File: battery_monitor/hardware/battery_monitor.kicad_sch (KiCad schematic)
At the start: 51 parts, among them J1 VEHICLE, J2 EXT_NTC, J3 DPDT_SENSE_POLE, U1 TPS7A1633AQDGNRQ1, U2 TLV7034QPWRQ1, U3 MDBT50Q-1MV2 (logical symbol)

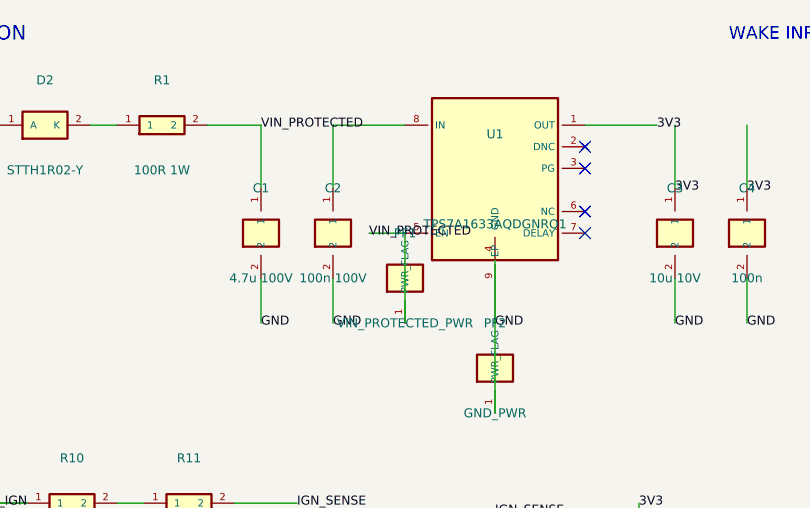
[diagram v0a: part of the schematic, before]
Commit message: Apply KiCad ERC fixes
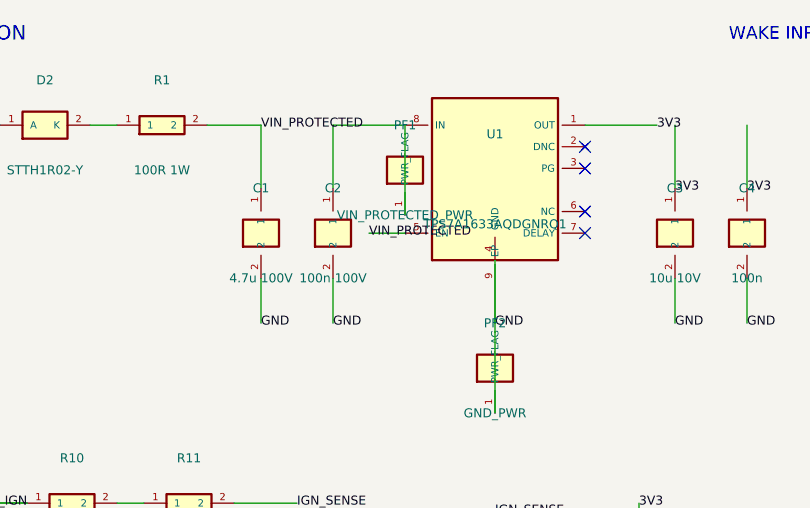
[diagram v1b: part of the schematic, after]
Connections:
- net VIN_PROTECTED: no longer PF1.1 (PWR_FLAG)
- net at C2.1, U1.8 (IN): now also PF1.1 (PWR_FLAG)
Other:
- moved on the sheet: PF1
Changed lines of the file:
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@@
   (wire (pts (xy 92 45) (xy 92 52)) (stroke (width 0) (type default)))
   (wire (pts (xy 92 48) (xy 92 52)) (stroke (width 0) (type default)))
-  (wire (pts (xy 82 42) (xy 82 52)) (stroke (width 0) (type default)))
+  (wire (pts (xy 82 30) (xy 82 40)) (stroke (width 0) (type default)))
   (wire (pts (xy 92 52) (xy 92 62)) (stroke (width 0) (type default)))
   (wire (pts (xy 112 37) (xy 112 30)) (stroke (width 0) (type default)))
@@
     (instances (project "battery_monitor" (path "/9c88e388-d519-50ad-aef0-ab628bb0a8df" (reference "U1") (unit 1))))
   )
-  (symbol (lib_id "BM:PWRFLAG") (at 82 47 0) (unit 1) (in_bom yes) (on_board yes)
-    (property "Reference" "PF1" (at 82 42 0) (effects (font (size 1.0 1.0))))
-    (property "Value" "VIN_PROTECTED_PWR" (at 82 52 0) (effects (font (size 1.0 1.0))))
-    (property "Footprint" "" (at 82 47 0) (effects (font (size 0.8 0.8)) hide))
-    (property "Datasheet" "" (at 82 47 0) (effects (font (size 0.8 0.8)) hide))
-    (property "Description" "" (at 82 47 0) (effects (font (size 0.8 0.8)) hide))
+  (symbol (lib_id "BM:PWRFLAG") (at 82 35 0) (unit 1) (in_bom yes) (on_board yes)
+    (property "Reference" "PF1" (at 82 30 0) (effects (font (size 1.0 1.0))))
+    (property "Value" "VIN_PROTECTED_PWR" (at 82 40 0) (effects (font (size 1.0 1.0))))
+    (property "Footprint" "" (at 82 35 0) (effects (font (size 0.8 0.8)) hide))
+    (property "Datasheet" "" (at 82 35 0) (effects (font (size 0.8 0.8)) hide))
+    (property "Description" "" (at 82 35 0) (effects (font (size 0.8 0.8)) hide))
     (pin "1")
     (instances (project "battery_monitor" (path "/9c88e388-d519-50ad-aef0-ab628bb0a8df" (reference "PF1") (unit 1))))

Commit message: Align KiCad schematic to grid and register libraries
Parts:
- removed C1: 4.7u 100V, Capacitor_SMD:C_1210_3225Metric, symbol BM:C
- removed C11, C12, C13, C14: 4.7n, Capacitor_SMD:C_0805_2012Metric, symbol BM:C
- removed C2: 100n 100V, Capacitor_SMD:C_0805_2012Metric, symbol BM:C
- removed C20: 10n, Capacitor_SMD:C_0805_2012Metric, symbol BM:C
- removed C3: 10u 10V, Capacitor_SMD:C_1206_3216Metric, symbol BM:C
- removed C4, C5: 100n, Capacitor_SMD:C_0805_2012Metric, symbol BM:C
- removed D1: SM50T30CAY, Diode_SMD:D_SMC, symbol BM:TVS
- removed D2: STTH1R02-Y, Diode_SMD:D_SOD-123F, symbol BM:DIODE
- removed D3, D4, D5, D6, D7: BAV199-Q, Package_TO_SOT_SMD:SOT-23, symbol BM:CLAMP3
- removed J1: VEHICLE, symbol BM:CONN6
- removed J2: EXT_NTC, symbol BM:CONN2
- removed J3: DPDT_SENSE_POLE, symbol BM:CONN2
- removed PF1: VIN_PROTECTED_PWR, symbol BM:PWRFLAG
- removed PF2: GND_PWR, symbol BM:PWRFLAG
- removed R1: 100R 1W, Resistor_SMD:R_2512_6332Metric, symbol BM:R
- removed R10, R11, R14, R15, R18, R19, R22, R23: 4.7M 1%, Resistor_SMD:R_1206_3216Metric, symbol BM:R
- removed R12, R16, R20, R24: 1.5M 1%, Resistor_SMD:R_1206_3216Metric, symbol BM:R
- removed R13, R17, R21, R25: 33M 1%, Resistor_SMD:R_1206_3216Metric, symbol BM:R
- removed R2: 3.9M 1%, Resistor_SMD:R_0805_2012Metric, symbol BM:R
- removed R3: 1.0M 1%, Resistor_SMD:R_0805_2012Metric, symbol BM:R
- removed R30, R31: 3.32M 1%, Resistor_SMD:R_1206_3216Metric, symbol BM:R
- removed R32: 806k 1%, Resistor_SMD:R_1206_3216Metric, symbol BM:R
- removed R40, R41: 10k 1%, Resistor_SMD:R_0805_2012Metric, symbol BM:R
- removed R42: 4.7M, Resistor_SMD:R_0805_2012Metric, symbol BM:R
- removed RT1: 10k NTC TBD, Resistor_SMD:R_0805_2012Metric, symbol BM:NTC
- removed U1: TPS7A1633AQDGNRQ1, symbol BM:LDO8
- removed U2: TLV7034QPWRQ1, Package_SO:TSSOP-14_4.4x5mm_P0.65mm, symbol BM:COMP4
- removed U3: MDBT50Q-1MV2 (logical symbol), symbol BM:MCU
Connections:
- no-connect marks 4 -> 0
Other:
- note removed: "BATTERY ADC"
- note removed: "Future REMOTE_START_OUT driver intentionally DNP / not designed yet"
- note removed: "Generated KiCad source; open/save in KiCad 10 and run ERC before PCB layout."
- note removed: "MCU / BLE"
- note removed: "POWER / AUTOMOTIVE PROTECTION"
- note removed: "Prototype schematic: input/power values frozen for first build; full Raytac footprint, connectors, remote-start driver, and PCB layout remain open."
- note removed: "REMOTE START PROVISION"
- note removed: "TEMPERATURE"
- note removed: "WAKE INPUT REFERENCE"
